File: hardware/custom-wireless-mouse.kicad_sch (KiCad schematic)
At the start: 34 parts, among them J1 SWD_HEADER, J2 B2B-XH-A, Q1 DMP2035U, SW1 JS202011SCQN, SW2 D2FC-F-7N(20M), SW3 D2FC-F-7N(20M), SW4 D2FC-F-7N(20M), SW5 D2FC-F-7N(20M), U1 nRF52810-QCAA-T, U2 PMW3610DM-SUDU, U3 TLV61220DBVT, Y1 NX2016SA-32MHZ

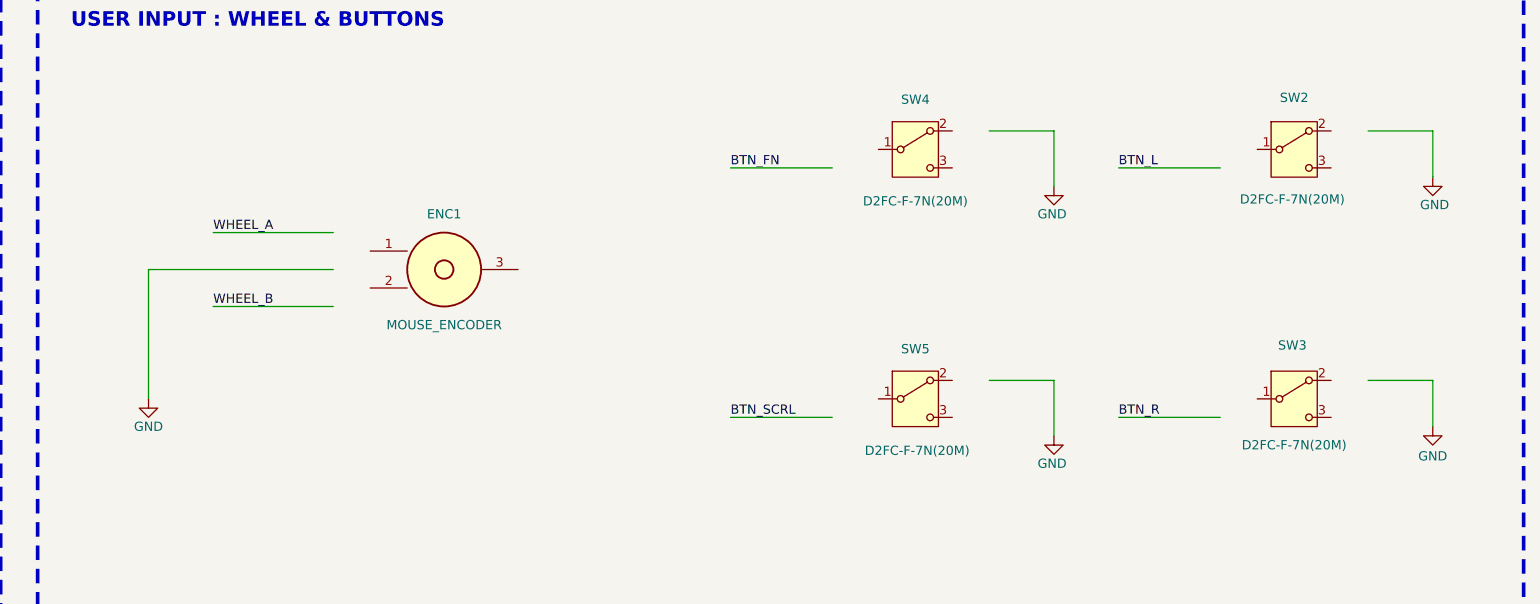
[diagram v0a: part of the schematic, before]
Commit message: Document User Input section as fully wired
ENC1 and SW2-SW5 are wired: WHEEL_A/WHEEL_B to the encoder, BTN_L/
BTN_R/BTN_FN/BTN_SCRL to their switches, all NO/COM pins to GND with
NC left open. BTN_SCRL runs on U1 pin 26 (P0.25); pin 12 (P0.15) is a
reserved spare alongside P0.00/P0.01/P0.28/P0.30. ERC: 0 errors, 0
warnings.
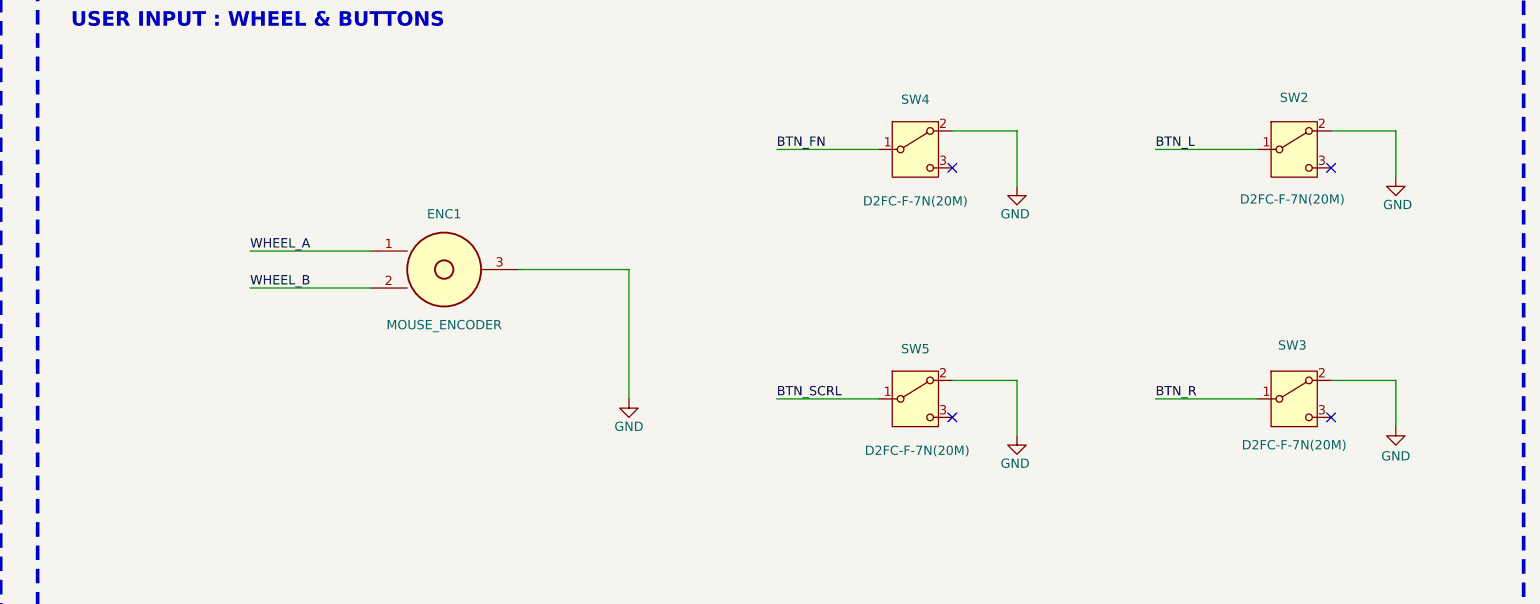
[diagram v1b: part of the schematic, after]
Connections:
- net BTN_FN: now also SW4.1 (COM)
- net BTN_L: now also SW2.1 (COM)
- net BTN_R: now also SW3.1 (COM)
- net BTN_SCRL: now also SW5.1 (COM)
- net GND: now also ENC1.3 (COM), SW2.2 (NO), SW3.2 (NO), SW4.2 (NO), SW5.2 (NO)
- net WHEEL_A: now also ENC1.1 (A)
- net WHEEL_B: now also ENC1.2 (B)
- no-connect marks 10 -> 14
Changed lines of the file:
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@@
 	)
 	(no_connect
+		(at 325.12 184.15)
+	)
+	(no_connect
+		(at 377.19 184.15)
+	)
+	(no_connect
 		(at 369.57 45.72)
 	)
@@
 	)
 	(no_connect
+		(at 325.12 218.44)
+	)
+	(no_connect
 		(at 78.74 59.69)
 	)
 	(no_connect
+		(at 377.19 218.44)
+	)
+	(no_connect
 		(at 369.57 48.26)
 	)
@@
 	(wire
 		(pts
-			(xy 391.16 213.36) (xy 391.16 219.71)
+			(xy 386.08 213.36) (xy 386.08 219.71)
 		)
 		(stroke
@@
 	(wire
 		(pts
-			(xy 223.52 203.2) (xy 240.03 203.2)
+			(xy 228.6 200.66) (xy 245.11 200.66)
 		)
 		(stroke
@@
 	(wire
 		(pts
+			(xy 280.67 198.12) (xy 280.67 215.9)
+		)
+		(stroke
+			(width 0)
+			(type default)
+		)
+	)
+	(wire
+		(pts
 			(xy 66.04 238.76) (xy 66.04 228.6)
 		)
@@
 	(wire
 		(pts
-			(xy 308.61 184.15) (xy 294.64 184.15)
+			(xy 314.96 181.61) (xy 300.99 181.61)
 		)
 		(stroke
@@
 	(wire
 		(pts
-			(xy 391.16 179.07) (xy 382.27 179.07)
+			(xy 386.08 179.07) (xy 377.19 179.07)
 		)
 		(stroke
@@
 	(wire
 		(pts
-			(xy 308.61 218.44) (xy 294.64 218.44)
+			(xy 314.96 215.9) (xy 300.99 215.9)
 		)
 		(stroke
@@
 	(wire
 		(pts
-			(xy 391.16 179.07) (xy 391.16 185.42)
+			(xy 386.08 179.07) (xy 386.08 185.42)
 		)
 		(stroke
@@
 	(wire
 		(pts
-			(xy 361.95 218.44) (xy 347.98 218.44)
+			(xy 367.03 215.9) (xy 353.06 215.9)
 		)
 		(stroke
@@
 	(wire
 		(pts
-			(xy 214.63 198.12) (xy 214.63 215.9)
-		)
-		(stroke
-			(width 0)
-			(type default)
-		)
-	)
-	(wire
-		(pts
 			(xy 285.75 67.31) (xy 285.75 68.58)
 		)
@@
 	(wire
 		(pts
-			(xy 391.16 213.36) (xy 382.27 213.36)
+			(xy 386.08 213.36) (xy 377.19 213.36)
 		)
 		(stroke
@@
 	(wire
 		(pts
-			(xy 339.09 179.07) (xy 330.2 179.07)
+			(xy 334.01 179.07) (xy 325.12 179.07)
 		)
 		(stroke
@@
 	(wire
 		(pts
-			(xy 361.95 184.15) (xy 347.98 184.15)
+			(xy 367.03 181.61) (xy 353.06 181.61)
 		)
 		(stroke
@@
 	(wire
 		(pts
-			(xy 339.09 179.07) (xy 339.09 186.69)
+			(xy 334.01 179.07) (xy 334.01 186.69)
 		)
 		(stroke
@@
 	(wire
 		(pts
-			(xy 339.09 213.36) (xy 339.09 220.98)
+			(xy 334.01 213.36) (xy 334.01 220.98)
 		)
 		(stroke
@@
 	(wire
 		(pts
-			(xy 240.03 198.12) (xy 214.63 198.12)
+			(xy 265.43 198.12) (xy 280.67 198.12)
 		)
 		(stroke
@@
 	(wire
 		(pts
-			(xy 339.09 213.36) (xy 330.2 213.36)
+			(xy 334.01 213.36) (xy 325.12 213.36)
 		)
 		(stroke
@@
 	(wire
 		(pts
-			(xy 223.52 193.04) (xy 240.03 193.04)
+			(xy 228.6 195.58) (xy 245.11 195.58)
 		)
 		(stroke
@@
 	)
 	(label "BTN_FN"
-		(at 294.64 184.15 0)
+		(at 300.99 181.61 0)
 		(effects
 			(font
@@
 	)
 	(label "WHEEL_A"
-		(at 223.52 193.04 0)
+		(at 228.6 195.58 0)
 		(effects
 			(font
@@
 	)
 	(label "BTN_L"
-		(at 347.98 184.15 0)
+		(at 353.06 181.61 0)
 		(effects
 			(font
@@
 	)
 	(label "BTN_R"
-		(at 347.98 218.44 0)
+		(at 353.06 215.9 0)
 		(effects
 			(font
@@
 	)
 	(label "WHEEL_B"
-		(at 223.52 203.2 0)
+		(at 228.6 200.66 0)
 		(effects
 			(font
@@
 	)
 	(label "BTN_SCRL"
-		(at 294.64 218.44 0)
+		(at 300.99 215.9 0)
 		(effects
 			(font
@@
 	(symbol
 		(lib_id "local:GND")
-		(at 339.09 220.98 0)
+		(at 334.01 220.98 0)
 		(unit 1)
 		(body_style 1)
@@
 		(dnp no)
 		(property "Reference" "#PWR049"
-			(at 339.09 218.44 0)
+			(at 334.01 218.44 0)
 			(hide yes)
 			(show_name no)
@@
 		)
 		(property "Value" "GND"
-			(at 338.836 224.79 0)
+			(at 333.756 224.79 0)
 			(show_name no)
 			(do_not_autoplace no)
@@
 		)
 		(property "Footprint" ""
-			(at 339.09 220.98 0)
+			(at 334.01 220.98 0)
 			(hide yes)
 			(show_name no)
@@
 		)
 		(property "Datasheet" ""
-			(at 339.09 220.98 0)
+			(at 334.01 220.98 0)
 			(hide yes)
 			(show_name no)
@@
 		)
 		(property "Description" ""
-			(at 339.09 220.98 0)
+			(at 334.01 220.98 0)
 			(show_name no)
 			(do_not_autoplace no)
@@
 	(symbol
 		(lib_id "local:GND")
-		(at 214.63 215.9 0)
+		(at 280.67 215.9 0)
+		(mirror y)
 		(unit 1)
 		(body_style 1)
@@
 		(dnp no)
 		(property "Reference" "#PWR034"
-			(at 214.63 213.36 0)
+			(at 280.67 213.36 0)
 			(hide yes)
 			(show_name no)
@@
 		)
 		(property "Value" "GND"
-			(at 214.63 219.71 0)
+			(at 280.67 219.71 0)
 			(show_name no)
 			(do_not_autoplace no)
@@
 		)
 		(property "Footprint" ""
-			(at 214.63 215.9 0)
+			(at 280.67 215.9 0)
 			(hide yes)
 			(show_name no)
@@
 		)
 		(property "Datasheet" ""
-			(at 214.63 215.9 0)
+			(at 280.67 215.9 0)
 			(hide yes)
 			(show_name no)
@@
 		)
 		(property "Description" ""
-			(at 214.63 215.9 0)
+			(at 280.67 215.9 0)
 			(show_name no)
 			(do_not_autoplace no)
@@
 	(symbol
 		(lib_id "local:GND")
-		(at 391.16 185.42 0)
+		(at 386.08 185.42 0)
 		(unit 1)
 		(body_style 1)
@@
 		(dnp no)
 		(property "Reference" "#PWR038"
-			(at 391.16 182.88 0)
+			(at 386.08 182.88 0)
 			(hide yes)
 			(show_name no)
@@
 		)
 		(property "Value" "GND"
-			(at 391.414 189.23 0)
+			(at 386.334 189.23 0)
 			(show_name no)
 			(do_not_autoplace no)
@@
 		)
 		(property "Footprint" ""
-			(at 391.16 185.42 0)
+			(at 386.08 185.42 0)
 			(hide yes)
 			(show_name no)
@@
 		)
 		(property "Datasheet" ""
-			(at 391.16 185.42 0)
+			(at 386.08 185.42 0)
 			(hide yes)
 			(show_name no)
@@
 		)
 		(property "Description" ""
-			(at 391.16 185.42 0)
+			(at 386.08 185.42 0)
 			(show_name no)
 			(do_not_autoplace no)
@@
 	(symbol
 		(lib_id "local:GND")
-		(at 339.09 186.69 0)
+		(at 334.01 186.69 0)
 		(unit 1)
 		(body_style 1)
@@
 		(dnp no)
 		(property "Reference" "#PWR040"
-			(at 339.09 184.15 0)
+			(at 334.01 184.15 0)
 			(hide yes)
 			(show_name no)
@@
 		)
 		(property "Value" "GND"
-			(at 338.836 190.5 0)
+			(at 333.756 190.5 0)
 			(show_name no)
 			(do_not_autoplace no)
@@
 		)
 		(property "Footprint" ""
-			(at 339.09 186.69 0)
+			(at 334.01 186.69 0)
 			(hide yes)
 			(show_name no)
@@
 		)
 		(property "Datasheet" ""
-			(at 339.09 186.69 0)
+			(at 334.01 186.69 0)
 			(hide yes)
 			(show_name no)
@@
 		)
 		(property "Description" ""
-			(at 339.09 186.69 0)
+			(at 334.01 186.69 0)
 			(show_name no)
 			(do_not_autoplace no)
@@
 	(symbol
 		(lib_id "local:GND")
-		(at 391.16 219.71 0)
+		(at 386.08 219.71 0)
 		(unit 1)
 		(body_style 1)
@@
 		(dnp no)
 		(property "Reference" "#PWR039"
-			(at 391.16 217.17 0)
+			(at 386.08 217.17 0)
 			(hide yes)
 			(show_name no)
@@
 		)
 		(property "Value" "GND"
-			(at 391.16 223.774 0)
+			(at 386.08 223.774 0)
 			(show_name no)
 			(do_not_autoplace no)
@@
 		)
 		(property "Footprint" ""
-			(at 391.16 219.71 0)
+			(at 386.08 219.71 0)
 			(hide yes)
 			(show_name no)
@@
 		)
 		(property "Datasheet" ""
-			(at 391.16 219.71 0)
+			(at 386.08 219.71 0)
 			(hide yes)
 			(show_name no)
@@
 		)
 		(property "Description" ""
-			(at 391.16 219.71 0)
+			(at 386.08 219.71 0)
 			(show_name no)
 			(do_not_autoplace no)

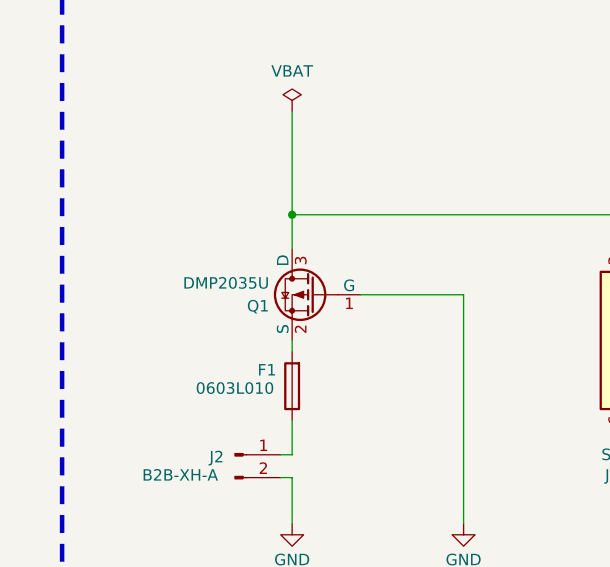
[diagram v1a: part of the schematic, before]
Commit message: Full BOM sourcing audit against Canadian distributors, swap Q1 to DMG2305UXQ
Every schematic component now carries verified Manufacturer/MPN/Distributor/
DPN fields, checked against DigiKey.ca as of 2026-09-27. Corrected several
components to their full orderable part numbers (Y1, F1, J2), fixed L1's
oversized placeholder footprint to match the real Murata part, and flagged
two live supply-chain risks (SW2-5 EOL, Q1 lead time) directly in the docs.

Q1 swapped from DMP2035U-7 (out of stock, 40-week lead) to DMG2305UXQ-7:
same SOT-23 pinout, in stock at DigiKey.ca, and a tighter gate threshold
(-0.9V max vs -1.0V) that narrows rather than widens the documented
near-dead-battery corner case. Vendored library, symbol, footprint, 3D
model, and datasheet all renamed/updated to match.

U2 and ENC1 sourcing confirmed through their actual mod-market/reseller
channels (AliExpress, Ausmodshop) since neither exists at standard
distributors — documented as a real characteristic of their supply chain,
not a gap.
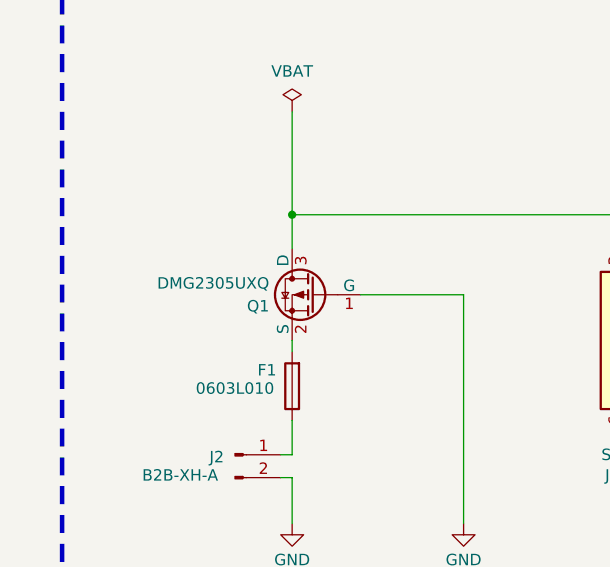
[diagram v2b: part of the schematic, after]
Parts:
- C1, C10, C14, C2, C3, C4, C9: DPN (none) -> 311-1344-1-ND; Distributor (none) -> DigiKey.ca; MPN (none) -> CC0603KRX7R9BB104; Manufacturer (none) -> Yageo
- C11, C5: DPN (none) -> 311-1443-1-ND; Distributor (none) -> DigiKey.ca; MPN (none) -> CC0603KRX5R6BB105; Manufacturer (none) -> Yageo
- C12, C15, C16, C8: DPN (none) -> 490-GRT188R61A106KE13JCT-ND; Distributor (none) -> DigiKey.ca; MPN (none) -> GRT188R61A106KE13J; Manufacturer (none) -> Murata
- C13: DPN (none) -> 311-1085-1-ND; Distributor (none) -> DigiKey.ca; MPN (none) -> CC0603KRX7R9BB103; Manufacturer (none) -> Yageo
- C6, C7: DPN (none) -> 311-1641-1-ND; Distributor (none) -> DigiKey.ca; MPN (none) -> CC0402FRNPO9BN120; Manufacturer (none) -> Yageo
- ENC1: DPN (none) -> N/A - see ATTRIBUTION.md; Distributor (none) -> Ausmodshop (mod-market retailer, not a standard electronics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; MPN (none) -> Mouse scroll encoder, 7-9mm body height (exact SKU varies b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; Manufacturer (none) -> TTC / Kailh (mod-market, unbranded)
- F1: DPN (none) -> F2900CT-ND; Distributor (none) -> DigiKey.ca; MPN (none) -> 0603L010YR; Manufacturer (none) -> Littelfuse
- J1: DPN (none) -> 612-TSW-104-07-T-S-ND; Distributor (none) -> DigiKey.ca; MPN (none) -> TSW-104-07-T-S; Manufacturer (none) -> Samtec
- J2: DPN (none) -> 455-B2B-XH-A-ND; Distributor (none) -> DigiKey.ca; MPN (none) -> B2B-XH-A(LF)(SN); Manufacturer (none) -> JST
- L1: footprint Inductor_SMD:L_1210_3225Metric -> Inductor_SMD:L_1008_2520Metric; DPN (none) -> 490-10577-1-ND; Distributor (none) -> DigiKey.ca; MPN (none) -> 1269AS-H-4R7M=P2; Manufacturer (none) -> Murata
- Q1: value DMP2035U -> DMG2305UXQ; footprint diodes-dmp2035u:sot-23-dmp2035u -> diodes-dmg2305uxq:sot-23-dmg2305uxq; symbol diodes-dmp2035u:DMP2035U -> diodes-dmg2305uxq:DMG2305UXQ; DPN (none) -> 31-DMG2305UXQ-7CT-ND; Distributor (none) -> DigiKey.ca; MPN (none) -> DMG2305UXQ-7; Manufacturer (none) -> Diodes Incorporated
- R1: DPN (none) -> 311-10.0KHRCT-ND; Distributor (none) -> DigiKey.ca; MPN (none) -> RC0603FR-0710KL; Manufacturer (none) -> Yageo
- R2: DPN (none) -> 311-499KHRCT-ND; Distributor (none) -> DigiKey.ca; MPN (none) -> RC0603FR-07499KL; Manufacturer (none) -> Yageo
- R3: DPN (none) -> 311-180KHRCT-ND; Distributor (none) -> DigiKey.ca; MPN (none) -> RC0603FR-07180KL; Manufacturer (none) -> Yageo
- SW1: DPN (none) -> 401-2002-1-ND; Distributor (none) -> DigiKey.ca; MPN (none) -> JS202011SCQN; Manufacturer (none) -> C&K (Littelfuse)
- SW2, SW3, SW4, SW5: DPN (none) -> 39-D2FC-F-7N(20M)-ND; Distributor (none) -> DigiKey.ca; MPN (none) -> D2FC-F-7N(20M); Manufacturer (none) -> Omron
- U1: DPN (none) -> 4823-NRF52810-QCAA-T-ND; Distributor (none) -> DigiKey.ca; MPN (none) -> nRF52810-QCAA-T; Manufacturer (none) -> Nordic Semiconductor
- U2: DPN (none) -> Item 1005007118767775; Distributor (none) -> AliExpress (specialty reseller, not a standard electronics 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; MPN (none) -> PMW3610DM-SUDU; Manufacturer (none) -> PixArt Imaging
- U3: DPN (none) -> 296-43576-1-ND; Distributor (none) -> DigiKey.ca; MPN (none) -> TLV61220DBVT; Manufacturer (none) -> Texas Instruments
- Y1: DPN (none) -> 644-CS06654-32MCT-ND; Distributor (none) -> DigiKey.ca; MPN (none) -> NX2016SA-32MHZ-EXS00A-CS06654; Manufacturer (none) -> NDK America
